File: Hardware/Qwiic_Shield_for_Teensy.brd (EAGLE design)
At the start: 17.8 x 61 mm, 42 parts, among them J1 QWIIC_RA, J2 QWIIC_RA, J3 QWIIC_Vertical, J4 QWIIC_Vertical, J5 ALT PWR

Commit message: Teensy FP library update
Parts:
- JP11: device Testing:TEENSY-3.1_NOSILK -> SparkFun-Boards:TEENSY-3.1_NOSILK
- moved JP11 19.9 mm to (8.89, 17.8)
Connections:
- new net 3V: JP11.3V
- new net VBAT: JP11.VBAT
- new net VIN: JP11.VIN
- new net VUSB: JP11.VUSB
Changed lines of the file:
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@@
 <drawing>
 <settings>
-<setting alwaysvectorfont="no"/>
+<setting alwaysvectorfont="yes"/>
 <setting verticaltext="up"/>
 </settings>
@@
 <layer number="45" name="Holes" color="7" fill="1" visible="yes" active="yes"/>
 <layer number="46" name="Milling" color="3" fill="1" visible="no" active="yes"/>
-<layer number="47" name="Measures" color="7" fill="1" visible="yes" active="yes"/>
+<layer number="47" name="Measures" color="7" fill="1" visible="no" active="yes"/>
 <layer number="48" name="Document" color="7" fill="1" visible="no" active="yes"/>
 <layer number="49" name="Reference" color="7" fill="1" visible="yes" active="yes"/>
@@
 <text x="6.35" y="0.381" size="1.27" layer="16" font="vector" ratio="15" rot="MR0" align="bottom-center">v10</text>
 <text x="13.97" y="-12.7" size="1.778" layer="51" font="vector">Pete Lewis</text>
-<wire x1="0" y1="35.814" x2="0" y2="60.96" width="0.127" layer="20"/>
-<wire x1="0" y1="60.96" x2="17.78" y2="60.96" width="0.127" layer="20"/>
-<wire x1="17.78" y1="60.96" x2="17.78" y2="35.814" width="0.127" layer="20"/>
-<wire x1="0" y1="0" x2="17.78" y2="0" width="0.127" layer="20"/>
-<wire x1="17.78" y1="0" x2="17.78" y2="35.306" width="0.127" layer="20"/>
-<wire x1="17.78" y1="35.814" x2="0" y2="35.814" width="0.127" layer="20"/>
-<wire x1="0" y1="35.306" x2="0" y2="0" width="0.127" layer="20"/>
-<wire x1="0" y1="35.306" x2="17.78" y2="35.306" width="0.127" layer="20"/>
+<wire x1="0" y1="35.814" x2="0" y2="60.96" width="0.2032" layer="20"/>
+<wire x1="0" y1="60.96" x2="17.78" y2="60.96" width="0.2032" layer="20"/>
+<wire x1="17.78" y1="60.96" x2="17.78" y2="35.814" width="0.2032" layer="20"/>
+<wire x1="0" y1="0" x2="17.78" y2="0" width="0.2032" layer="20"/>
+<wire x1="17.78" y1="0" x2="17.78" y2="35.306" width="0.2032" layer="20"/>
+<wire x1="17.78" y1="35.814" x2="0" y2="35.814" width="0.2032" layer="20"/>
+<wire x1="0" y1="35.306" x2="0" y2="0" width="0.2032" layer="20"/>
+<wire x1="0" y1="35.306" x2="17.78" y2="35.306" width="0.2032" layer="20"/>
 <dimension x1="0" y1="0" x2="0" y2="60.96" x3="-22.86" y3="30.48" textsize="1.778" layer="47" unit="inch" visible="yes"/>
 <dimension x1="0" y1="0" x2="0" y2="35.56" x3="-17.78" y3="17.78" textsize="1.778" layer="47" unit="inch" visible="yes"/>
@@
 <element name="FD4" library="SparkFun-Aesthetics" package="FIDUCIAL-1X2" value="FIDUCIAL1X2" x="14.986" y="32.766" smashed="yes" rot="MR0"/>
 <element name="U$3" library="buzzard_labels (24)" package="3V36" value="" x="0" y="0" smashed="yes"/>
-<element name="JP11" library="Testing" package="TEENSY-3.1_NOSILK" value="TEENSY" x="0" y="0" smashed="yes">
-<attribute name="NAME" x="5.08" y="36.83" size="1.27" layer="25"/>
+<element name="JP11" library="SparkFun-Boards" package="TEENSY-3.1_NOSILK" value="TEENSY" x="8.89" y="17.78" smashed="yes">
+<attribute name="NAME" x="13.97" y="54.61" size="1.27" layer="25"/>
+<attribute name="SF_ID" value="DEV-12646" x="8.89" y="17.78" size="1.778" layer="27" display="off"/>
 </element>
 <element name="R3" library="SparkFun-Resistors" package="0603" value="4.7k" x="13.97" y="15.24" smashed="yes" rot="R270">
@@
 <wire x1="9.39" y1="5.08" x2="9.39" y2="7.103" width="0.254" layer="1"/>
 <wire x1="9.39" y1="7.103" x2="9.412" y2="7.125" width="0.254" layer="1"/>
-<wire x1="1.27" y1="21.59" x2="7.493" y2="21.59" width="0.254" layer="1"/>
 <wire x1="8.39" y1="20.693" x2="8.39" y2="16.51" width="0.254" layer="1"/>
-<wire x1="7.493" y1="21.59" x2="8.39" y2="20.693" width="0.254" layer="1"/>
+<wire x1="7.5565" y1="21.5265" x2="8.39" y2="20.693" width="0.254" layer="1"/>
 <wire x1="8.39" y1="16.51" x2="8.39" y2="14.487" width="0.254" layer="1"/>
 <wire x1="8.39" y1="14.487" x2="8.368" y2="14.465" width="0.254" layer="1"/>
@@
 <wire x1="9.6266" y1="12.0904" x2="8.39" y2="12.0904" width="0.254" layer="1"/>
 <wire x1="11.049" y1="13.5128" x2="9.6266" y2="12.0904" width="0.254" layer="1"/>
+<wire x1="1.27" y1="21.59" x2="7.493" y2="21.59" width="0.254" layer="1"/>
+<wire x1="7.493" y1="21.59" x2="7.5565" y2="21.5265" width="0.254" layer="1"/>
 </signal>
 <signal name="SCL">
@@
 <wire x1="7.39" y1="16.51" x2="7.39" y2="14.487" width="0.254" layer="1"/>
 <wire x1="7.39" y1="14.487" x2="7.368" y2="14.465" width="0.254" layer="1"/>
-<wire x1="1.905" y1="18.415" x2="1.27" y2="19.05" width="0.254" layer="1"/>
-<wire x1="6.8834" y1="18.415" x2="1.905" y2="18.415" width="0.254" layer="1"/>
+<wire x1="1.44318125" y1="18.415" x2="1.27" y2="19.05" width="0.254" layer="1"/>
+<wire x1="6.8834" y1="18.415" x2="1.44318125" y2="18.415" width="0.254" layer="1"/>
 <wire x1="13.97" y1="16.09" x2="12.8134" y2="16.09" width="0.254" layer="1"/>
 <wire x1="12.8134" y1="16.09" x2="12.192" y2="15.4686" width="0.254" layer="1"/>
@@
 <contactref element="JP11" pad="3.3V"/>
 <contactref element="3V3_ISO" pad="2"/>
-<wire x1="11.4173" y1="28.067" x2="11.4173" y2="34.2773" width="0.508" layer="16"/>
-<wire x1="11.4173" y1="34.2773" x2="11.43" y2="34.29" width="0.508" layer="16"/>
+<wire x1="11.4173" y1="28.067" x2="11.4173" y2="34.338875" width="0.508" layer="16"/>
+<wire x1="11.4173" y1="34.338875" x2="11.43" y2="34.29" width="0.508" layer="16"/>
 </signal>
 <signal name="N$4">
@@
 <wire x1="6.35" y1="32.639" x2="6.096" y2="32.385" width="0.254" layer="1"/>
 </signal>
+<signal name="VBAT">
+<contactref element="JP11" pad="VBAT"/>
+</signal>
+<signal name="3V">
+<contactref element="JP11" pad="3V"/>
+</signal>
+<signal name="VIN">
+<contactref element="JP11" pad="VIN"/>
+</signal>
+<signal name="VUSB">
+<contactref element="JP11" pad="VUSB"/>
+</signal>
 </signals>

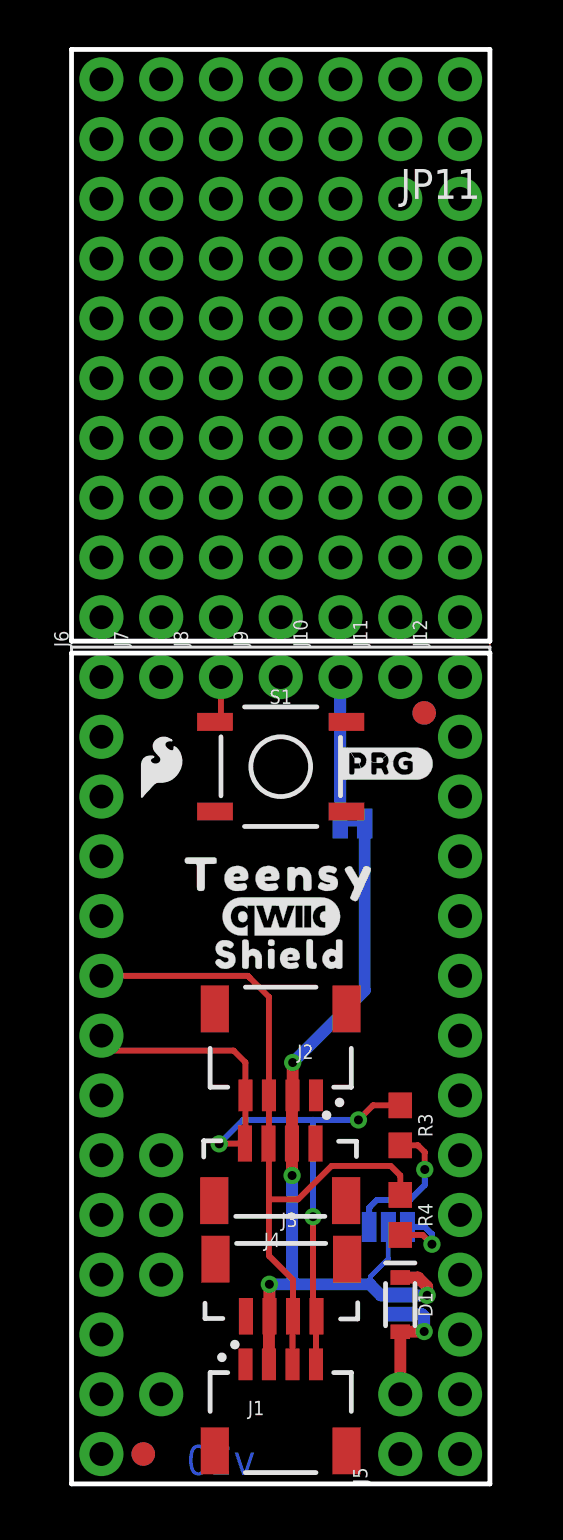
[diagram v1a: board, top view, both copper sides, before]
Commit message: DRC approvals, label adjustments
-bumped GND pour isolates to 0.008 inch. This allows AREF pin to still get flowed gnd.
-approved DRC errors about dimension on vscore line
-fixed some angled traces.
-removed some trace stubs
-rotated SDA and SCL to match orientation of other labels
-ensures all labels were size 0.04
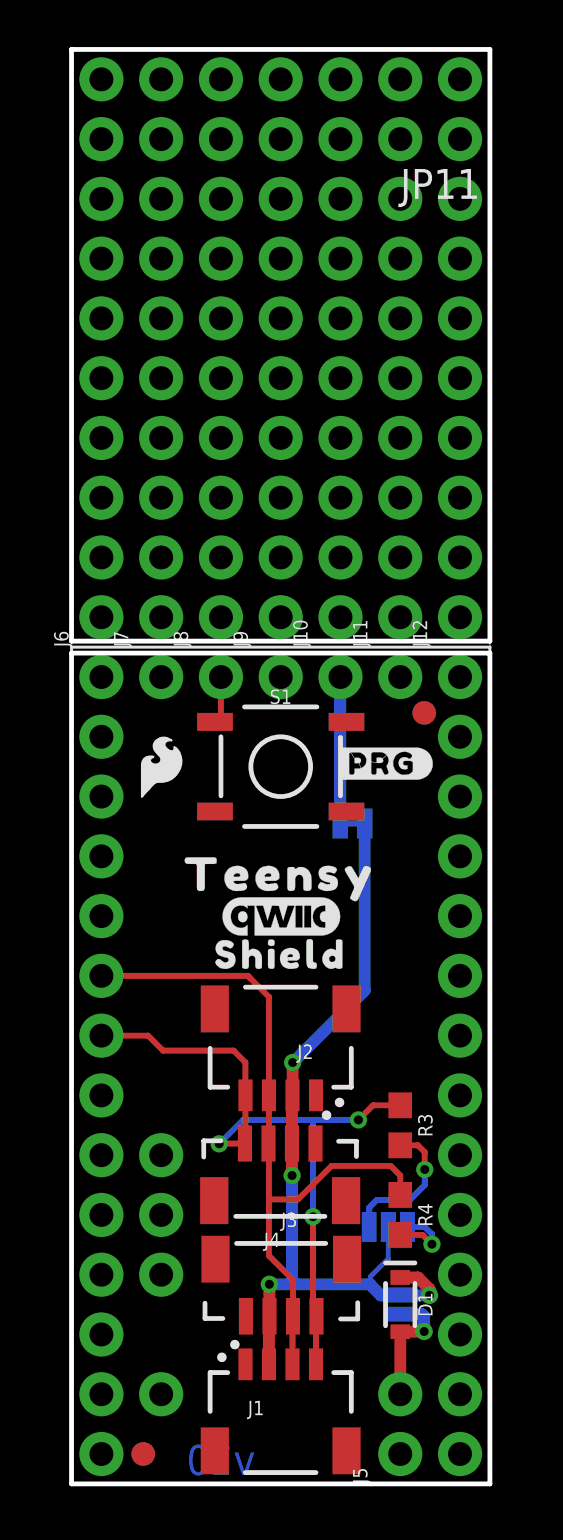
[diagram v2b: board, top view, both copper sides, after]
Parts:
- turned U$19 to 0 degrees
- turned U$18 to 0 degrees
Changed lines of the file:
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@@
 <element name="U$15" library="output" package="#3V3#0" value="" x="11.43" y="33.782" smashed="yes" rot="MR270"/>
 <element name="U$17" library="output" package="#GND#0" value="" x="8.89" y="31.496" smashed="yes" rot="MR270"/>
-<element name="U$18" library="output" package="#SDA#0" value="" x="1.778" y="21.59" smashed="yes" rot="MR180"/>
-<element name="U$19" library="output" package="#SCL#0" value="" x="1.778" y="19.05" smashed="yes" rot="MR180"/>
+<element name="U$18" library="output" package="#SDA#0" value="" x="1.778" y="21.59" smashed="yes" rot="MR0"/>
+<element name="U$19" library="output" package="#SCL#0" value="" x="1.7526" y="19.0754" smashed="yes" rot="MR0"/>
 <element name="J5" library="SparkFun-Connectors" package="1X02_NO_SILK" value="ALT PWR" x="13.97" y="1.27" smashed="yes" rot="R90">
 <attribute name="NAME" x="12.573" y="0" size="0.6096" layer="25" font="vector" ratio="20" rot="R90"/>
@@
 <contactref element="J2" pad="1"/>
 <contactref element="J1" pad="1"/>
-<polygon width="0.2032" layer="1">
+<polygon width="0.2032" layer="1" isolate="0.2032">
 <vertex x="0" y="0"/>
 <vertex x="17.78" y="0"/>
@@
 <vertex x="0" y="60.96"/>
 </polygon>
-<polygon width="0.2032" layer="16">
+<polygon width="0.2032" layer="16" isolate="0.2032">
 <vertex x="17.78" y="0"/>
 <vertex x="0" y="0"/>
@@
 <via x="9.398" y="17.907" extent="1-16" drill="0.381"/>
 <wire x1="13.97" y1="8.77" x2="14.725" y2="8.77" width="0.508" layer="1"/>
-<wire x1="15.113" y1="8.382" x2="15.113" y2="8.0137" width="0.508" layer="1"/>
-<via x="15.113" y="8.0137" extent="1-16" drill="0.381"/>
-<wire x1="15.113" y1="8.0137" x2="13.9827" y2="8.0137" width="0.508" layer="16"/>
+<wire x1="15.2146" y1="8.2804" x2="15.2146" y2="8.0137" width="0.508" layer="1"/>
+<via x="15.2146" y="8.0137" extent="1-16" drill="0.381"/>
+<wire x1="15.2146" y1="8.0137" x2="13.9827" y2="8.0137" width="0.508" layer="16"/>
 <wire x1="13.9827" y1="8.0137" x2="13.97" y2="8.0264" width="0.508" layer="16"/>
-<wire x1="14.725" y1="8.77" x2="15.113" y2="8.382" width="0.508" layer="1"/>
+<wire x1="14.725" y1="8.77" x2="15.2146" y2="8.2804" width="0.508" layer="1"/>
 <wire x1="8.39" y1="5.08" x2="8.39" y2="7.103" width="0.508" layer="1"/>
 <wire x1="8.39" y1="7.103" x2="8.412" y2="7.125" width="0.508" layer="1"/>
@@
 <wire x1="8.412" y1="8.479" x2="8.4074" y2="8.4836" width="0.508" layer="1"/>
 <via x="8.4074" y="8.4836" extent="1-16" drill="0.381"/>
-<wire x1="13.97" y1="8.001" x2="13.9827" y2="8.0137" width="0.2032" layer="16"/>
 <wire x1="9.3726" y1="8.4836" x2="12.6746" y2="8.4836" width="0.508" layer="16"/>
 <wire x1="12.7" y1="8.4836" x2="12.6746" y2="8.4836" width="0.508" layer="16"/>
@@
 <wire x1="7.39" y1="16.51" x2="7.39" y2="14.487" width="0.254" layer="1"/>
 <wire x1="7.39" y1="14.487" x2="7.368" y2="14.465" width="0.254" layer="1"/>
-<wire x1="1.44318125" y1="18.415" x2="1.27" y2="19.05" width="0.254" layer="1"/>
-<wire x1="6.8834" y1="18.415" x2="1.44318125" y2="18.415" width="0.254" layer="1"/>
 <wire x1="13.97" y1="16.09" x2="12.8134" y2="16.09" width="0.254" layer="1"/>
 <wire x1="12.8134" y1="16.09" x2="12.192" y2="15.4686" width="0.254" layer="1"/>
@@
 <wire x1="6.2862" y1="14.465" x2="7.368" y2="14.465" width="0.254" layer="1"/>
 <wire x1="10.2616" y1="11.3538" x2="10.2616" y2="15.4686" width="0.254" layer="16"/>
+<wire x1="3.2512" y1="19.05" x2="1.27" y2="19.05" width="0.254" layer="1"/>
+<wire x1="6.8834" y1="18.415" x2="3.8862" y2="18.415" width="0.254" layer="1"/>
+<wire x1="3.8862" y1="18.415" x2="3.2512" y2="19.05" width="0.254" layer="1"/>
 </signal>
 <signal name="N$1">
@@
 <contactref element="JP11" pad="3.3V"/>
 <contactref element="3V3_ISO" pad="2"/>
-<wire x1="11.4173" y1="28.067" x2="11.4173" y2="34.338875" width="0.508" layer="16"/>
-<wire x1="11.4173" y1="34.338875" x2="11.43" y2="34.29" width="0.508" layer="16"/>
+<wire x1="11.4173" y1="28.067" x2="11.4173" y2="34.2773" width="0.508" layer="16"/>
+<wire x1="11.4173" y1="34.2773" x2="11.43" y2="34.29" width="0.508" layer="16"/>
 </signal>
 <signal name="N$4">
@@
 <mfgpreviewcolor name="substratecolor" color="0xFF786E46"/>
 </mfgpreviewcolors>
+<errors>
+</errors>
 </board>
 </drawing>
